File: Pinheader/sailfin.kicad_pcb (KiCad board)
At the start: 2 copper layers, 95.5 x 93 mm, 191 parts, among them J1 AnalogIn, J19 Barrel_Jack_Switch, J2 ATO1, J3 Raspberry_Pi_2_3, J4 Conn_02x25_Odd_Even, J5 i2c, J6 Screw_Terminal_01x02, J7 1wire, J8 PwmOut, J9 AnalogOut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

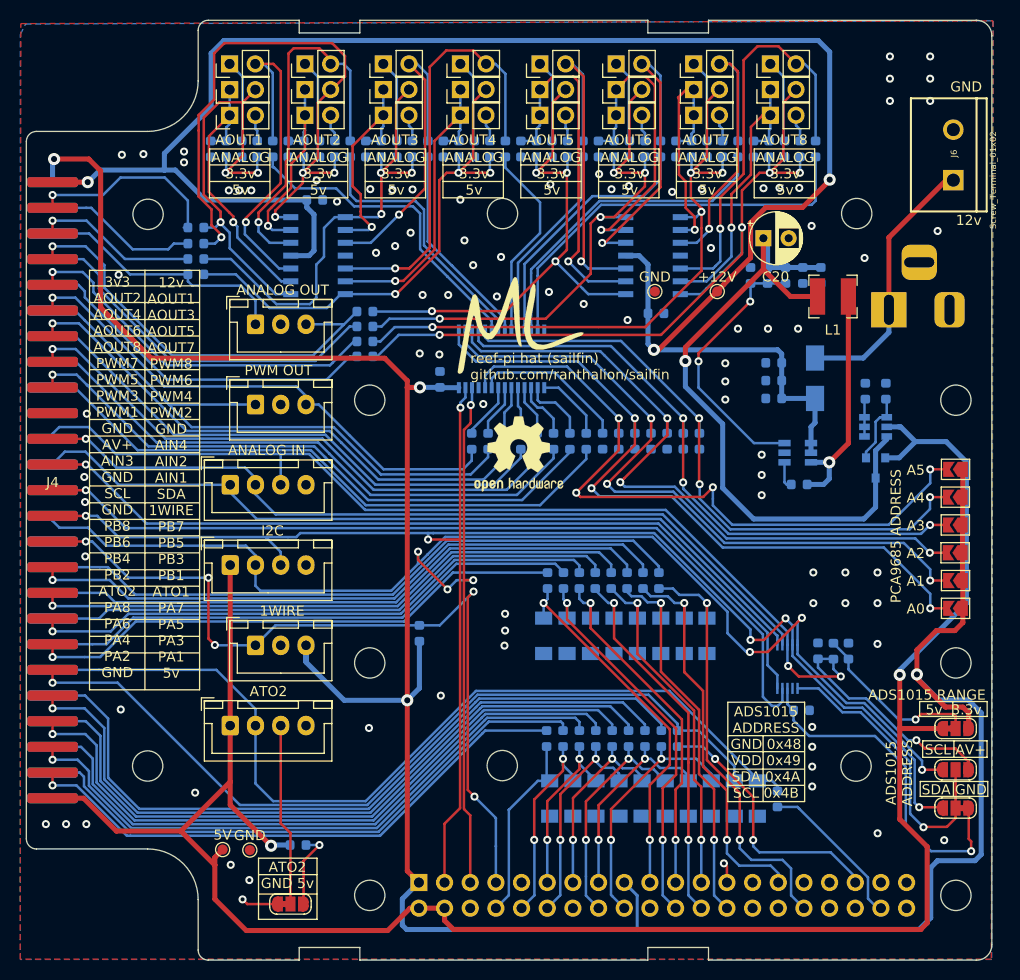
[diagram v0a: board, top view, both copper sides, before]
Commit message: card edge revision
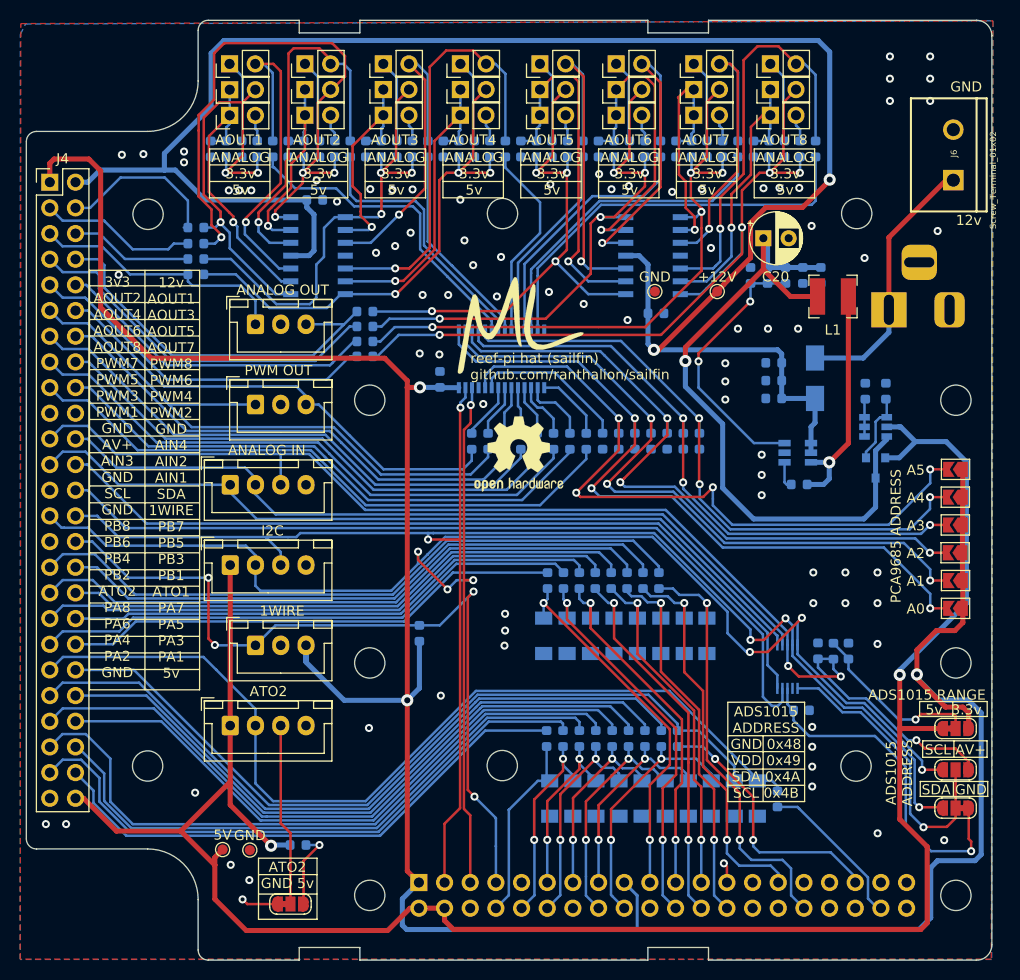
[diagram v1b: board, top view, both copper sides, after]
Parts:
- J4: footprint ml_footprints:Edge Connector 50 pin -> Connector_PinHeader_2.54mm:PinHeader_2x25_P2.54mm_Vertical
- moved J4 29.2 mm to (18.8, 114.3)
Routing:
- net /PA7: track 73.2 -> 67.2 mm, vias 1 -> 0
- net /PA5: track 68.1 -> 62.9 mm, vias 1 -> 0
- net /AOUT7: track 36.7 -> 32.1 mm, vias 1 -> 0
- net /PWM2: track 60.0 -> 55.8 mm, vias 1 -> 0
- net /AOUT3: track 16.2 -> 12.2 mm, vias 1 -> 0
- net /PWM8: track 51.8 -> 47.7 mm, vias 1 -> 0
- net /PWM6: track 54.2 -> 50.1 mm, vias 1 -> 0
- net /AOUT5: track 43.7 -> 39.7 mm, vias 1 -> 0
- net /PWM4: track 57.2 -> 53.2 mm, vias 1 -> 0
- net /PB3: track 57.3 -> 53.2 mm, vias 1 -> 0
- net /PB1: track 53.7 -> 49.6 mm, vias 1 -> 0
- net /PB7: track 64.3 -> 61.3 mm, vias 1 -> 0
- net /ATO1: track 83.0 -> 80.0 mm, vias 1 -> 0
- net /PB5: track 60.1 -> 57.1 mm, vias 1 -> 0
- net /AOUT1: track 19.4 -> 16.4 mm, vias 1 -> 0
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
